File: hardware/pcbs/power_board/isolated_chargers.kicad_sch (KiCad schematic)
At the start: 9 parts, among them Q1 BSS138

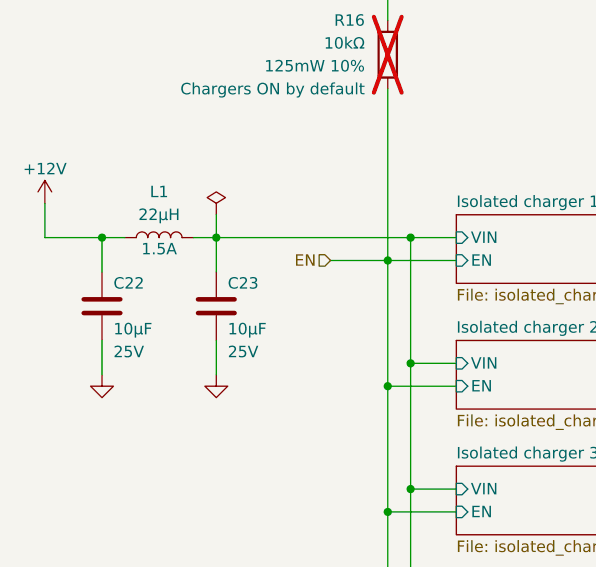
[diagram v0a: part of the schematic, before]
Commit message: power_board: arrange stuff on board
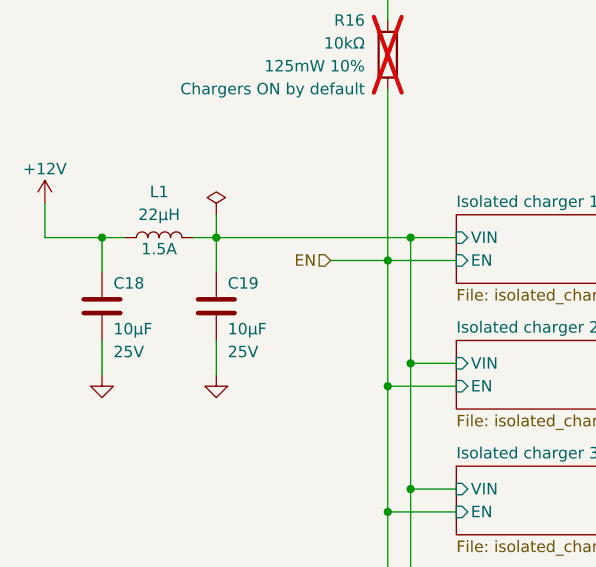
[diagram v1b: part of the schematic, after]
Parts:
- renumbered C22 to C18, C23 to C19
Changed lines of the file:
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@@
 		(dnp no)
 		(fields_autoplaced yes)
-		(property "Reference" "#PWR028"
+		(property "Reference" "#PWR024"
 			(at 160.02 78.74 0)
 			(effects
@@
 			(project "power_board"
 				(path "/4b166175-80a4-48c6-994d-6e62a6160b87/2e2b9578-5dbd-4b2d-88fb-256ac9c8dd75"
-					(reference "#PWR028")
+					(reference "#PWR024")
 					(unit 1)
 				)
@@
 		(on_board yes)
 		(dnp no)
-		(property "Reference" "C23"
+		(property "Reference" "C19"
 			(at 88.9 106.68 0)
 			(effects
@@
 			(project "power_board"
 				(path "/4b166175-80a4-48c6-994d-6e62a6160b87/2e2b9578-5dbd-4b2d-88fb-256ac9c8dd75"
-					(reference "C23")
+					(reference "C19")
 					(unit 1)
 				)
@@
 		(on_board yes)
 		(dnp no)
-		(property "Reference" "#PWR029"
+		(property "Reference" "#PWR025"
 			(at 185.42 78.74 0)
 			(effects
@@
 			(project "power_board"
 				(path "/4b166175-80a4-48c6-994d-6e62a6160b87/2e2b9578-5dbd-4b2d-88fb-256ac9c8dd75"
-					(reference "#PWR029")
+					(reference "#PWR025")
 					(unit 1)
 				)
@@
 		(dnp no)
 		(fields_autoplaced yes)
-		(property "Reference" "#PWR027"
+		(property "Reference" "#PWR023"
 			(at 106.68 172.72 0)
 			(effects
@@
 			(project "power_board"
 				(path "/4b166175-80a4-48c6-994d-6e62a6160b87/2e2b9578-5dbd-4b2d-88fb-256ac9c8dd75"
-					(reference "#PWR027")
+					(reference "#PWR023")
 					(unit 1)
 				)
@@
 		(dnp no)
 		(fields_autoplaced yes)
-		(property "Reference" "#PWR030"
+		(property "Reference" "#PWR026"
 			(at 185.42 114.3 0)
 			(effects
@@
 			(project "power_board"
 				(path "/4b166175-80a4-48c6-994d-6e62a6160b87/2e2b9578-5dbd-4b2d-88fb-256ac9c8dd75"
-					(reference "#PWR030")
+					(reference "#PWR026")
 					(unit 1)
 				)
@@
 		(on_board yes)
 		(dnp no)
-		(property "Reference" "#PWR026"
+		(property "Reference" "#PWR022"
 			(at 106.68 78.74 0)
 			(effects
@@
 			(project "power_board"
 				(path "/4b166175-80a4-48c6-994d-6e62a6160b87/2e2b9578-5dbd-4b2d-88fb-256ac9c8dd75"
-					(reference "#PWR026")
+					(reference "#PWR022")
 					(unit 1)
 				)
@@
 		(dnp no)
 		(fields_autoplaced yes)
-		(property "Reference" "#PWR024"
+		(property "Reference" "#PWR020"
 			(at 74.93 123.19 0)
 			(effects
@@
 			(project "power_board"
 				(path "/4b166175-80a4-48c6-994d-6e62a6160b87/2e2b9578-5dbd-4b2d-88fb-256ac9c8dd75"
-					(reference "#PWR024")
+					(reference "#PWR020")
 					(unit 1)
 				)
@@
 		(on_board yes)
 		(dnp no)
-		(property "Reference" "C22"
+		(property "Reference" "C18"
 			(at 76.2 106.68 0)
 			(effects
@@
 			(project "power_board"
 				(path "/4b166175-80a4-48c6-994d-6e62a6160b87/2e2b9578-5dbd-4b2d-88fb-256ac9c8dd75"
-					(reference "C22")
+					(reference "C18")
 					(unit 1)
 				)
@@
 		(dnp no)
 		(fields_autoplaced yes)
-		(property "Reference" "#PWR025"
+		(property "Reference" "#PWR021"
 			(at 87.63 123.19 0)
 			(effects
@@
 			(project "power_board"
 				(path "/4b166175-80a4-48c6-994d-6e62a6160b87/2e2b9578-5dbd-4b2d-88fb-256ac9c8dd75"
-					(reference "#PWR025")
+					(reference "#PWR021")
 					(unit 1)
 				)
@@
 		(on_board yes)
 		(dnp no)
-		(property "Reference" "#PWR023"
+		(property "Reference" "#PWR019"
 			(at 68.58 101.6 0)
 			(effects
@@
 			(project "power_board"
 				(path "/4b166175-80a4-48c6-994d-6e62a6160b87/2e2b9578-5dbd-4b2d-88fb-256ac9c8dd75"
-					(reference "#PWR023")
-					(unit 1)
-				)
+					(reference "#PWR019")
+					(unit 1)
+				)

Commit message: power_board: final version
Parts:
- C18, C19: LCSC (none) -> C15850
- L1: LCSC (none) -> C223014
- Q1: LCSC (none) -> C7420339
- R16, R17, R20: LCSC (none) -> C17414
- R18: LCSC (none) -> C17673
- R19: LCSC (none) -> C17415
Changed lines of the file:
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@@
+			)
+		)
+		(property "LCSC" "C7420339"
+			(at 182.88 101.6 0)
+			(effects
+				(font
+					(size 1.27 1.27)
+				)
+				(hide yes)
 			)
 		)
@@
 		)
 		(property "Shop" "https://store.comet.bg/Catalogue/Product/29580/"
+			(at 170.18 101.6 0)
+			(effects
+				(font
+					(size 1.27 1.27)
+				)
+				(hide yes)
+			)
+		)
+		(property "LCSC" "C17415"
 			(at 170.18 101.6 0)
 			(effects
@@
 			)
 		)
+		(property "LCSC" "C17414"
+			(at 106.68 160.02 0)
+			(effects
+				(font
+					(size 1.27 1.27)
+				)
+				(hide yes)
+			)
+		)
 		(pin "1"
 		)
@@
 		)
 		(property "Shop" "https://store.comet.bg/Catalogue/Product/44616/"
+			(at 87.63 109.22 0)
+			(effects
+				(font
+					(size 1.27 1.27)
+				)
+				(hide yes)
+			)
+		)
+		(property "LCSC" "C15850"
 			(at 87.63 109.22 0)
 			(effects
@@
 			)
 		)
+		(property "LCSC" "C17414"
+			(at 185.42 81.28 0)
+			(effects
+				(font
+					(size 1.27 1.27)
+				)
+				(hide yes)
+			)
+		)
 		(pin "1"
 		)
@@
 			)
 		)
+		(property "LCSC" "C15850"
+			(at 74.93 109.22 0)
+			(effects
+				(font
+					(size 1.27 1.27)
+				)
+				(hide yes)
+			)
+		)
 		(pin "1"
 		)
@@
 			)
 		)
+		(property "LCSC" "C17414"
+			(at 106.68 81.28 0)
+			(effects
+				(font
+					(size 1.27 1.27)
+				)
+				(hide yes)
+			)
+		)
 		(pin "1"
 		)
@@
 			)
 		)
+		(property "LCSC" "C17673"
+			(at 160.02 81.28 0)
+			(effects
+				(font
+					(size 1.27 1.27)
+				)
+				(hide yes)
+			)
+		)
 		(pin "1"
 		)
@@
 			)
 		)
+		(property "LCSC" "C223014"
+			(at 81.28 101.6 0)
+			(effects
+				(font
+					(size 1.27 1.27)
+				)
+				(hide yes)
+			)
+		)

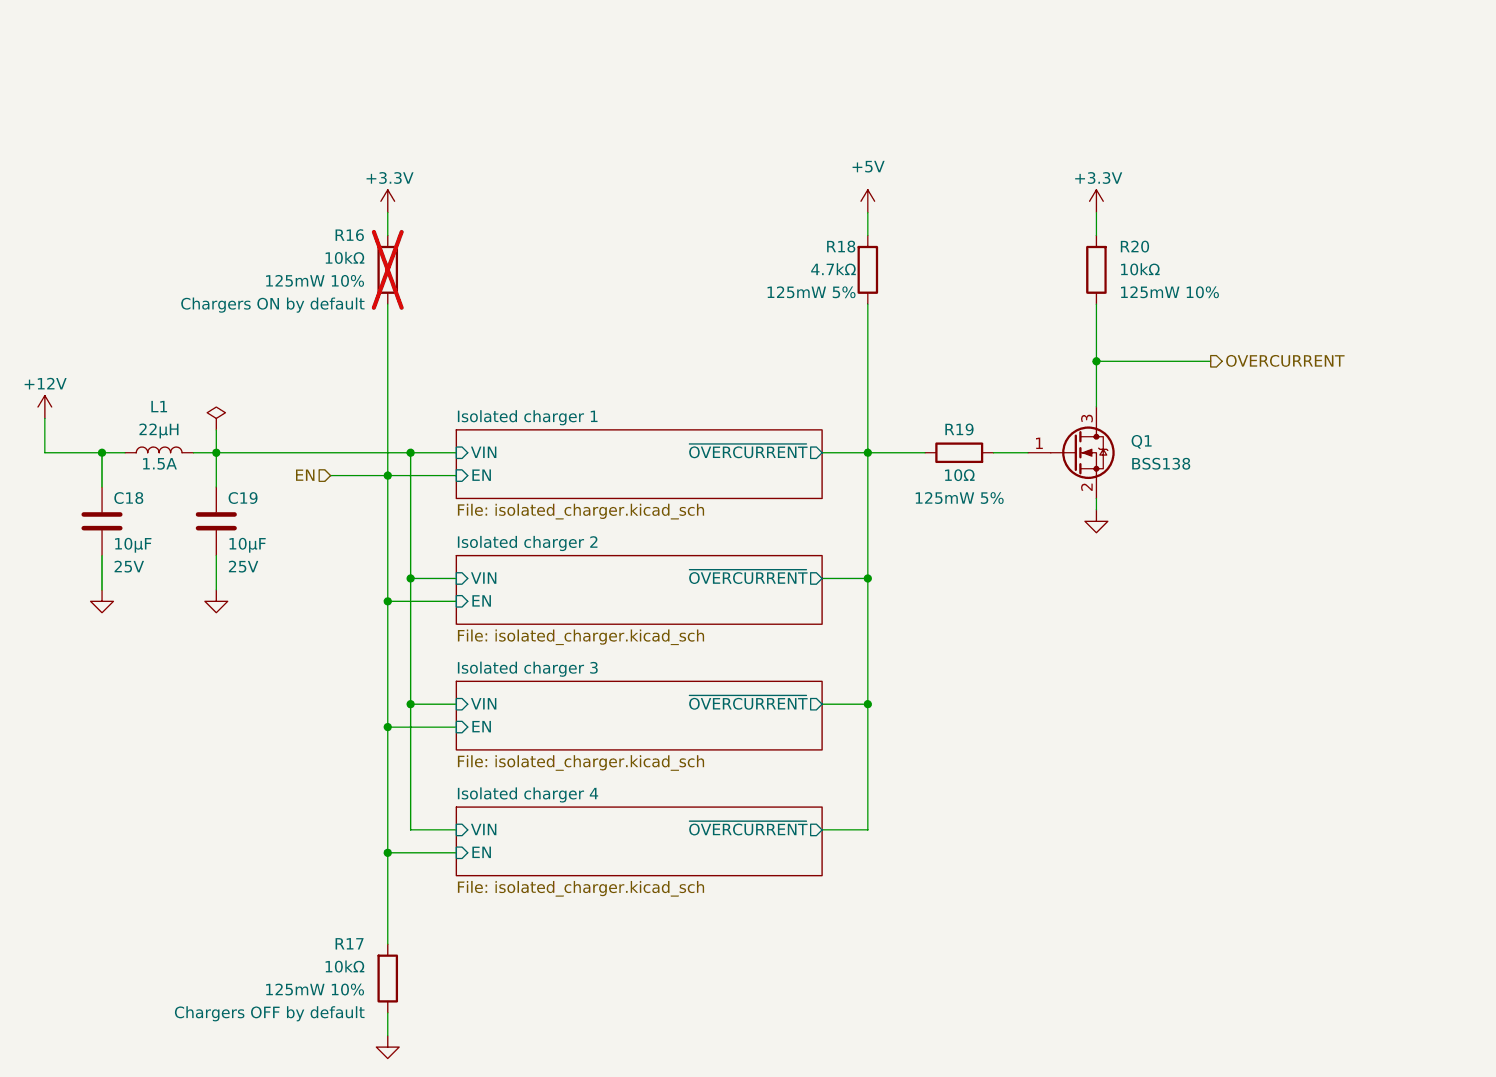
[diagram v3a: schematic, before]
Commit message: power_board: nuke general purpose leds and power cycler
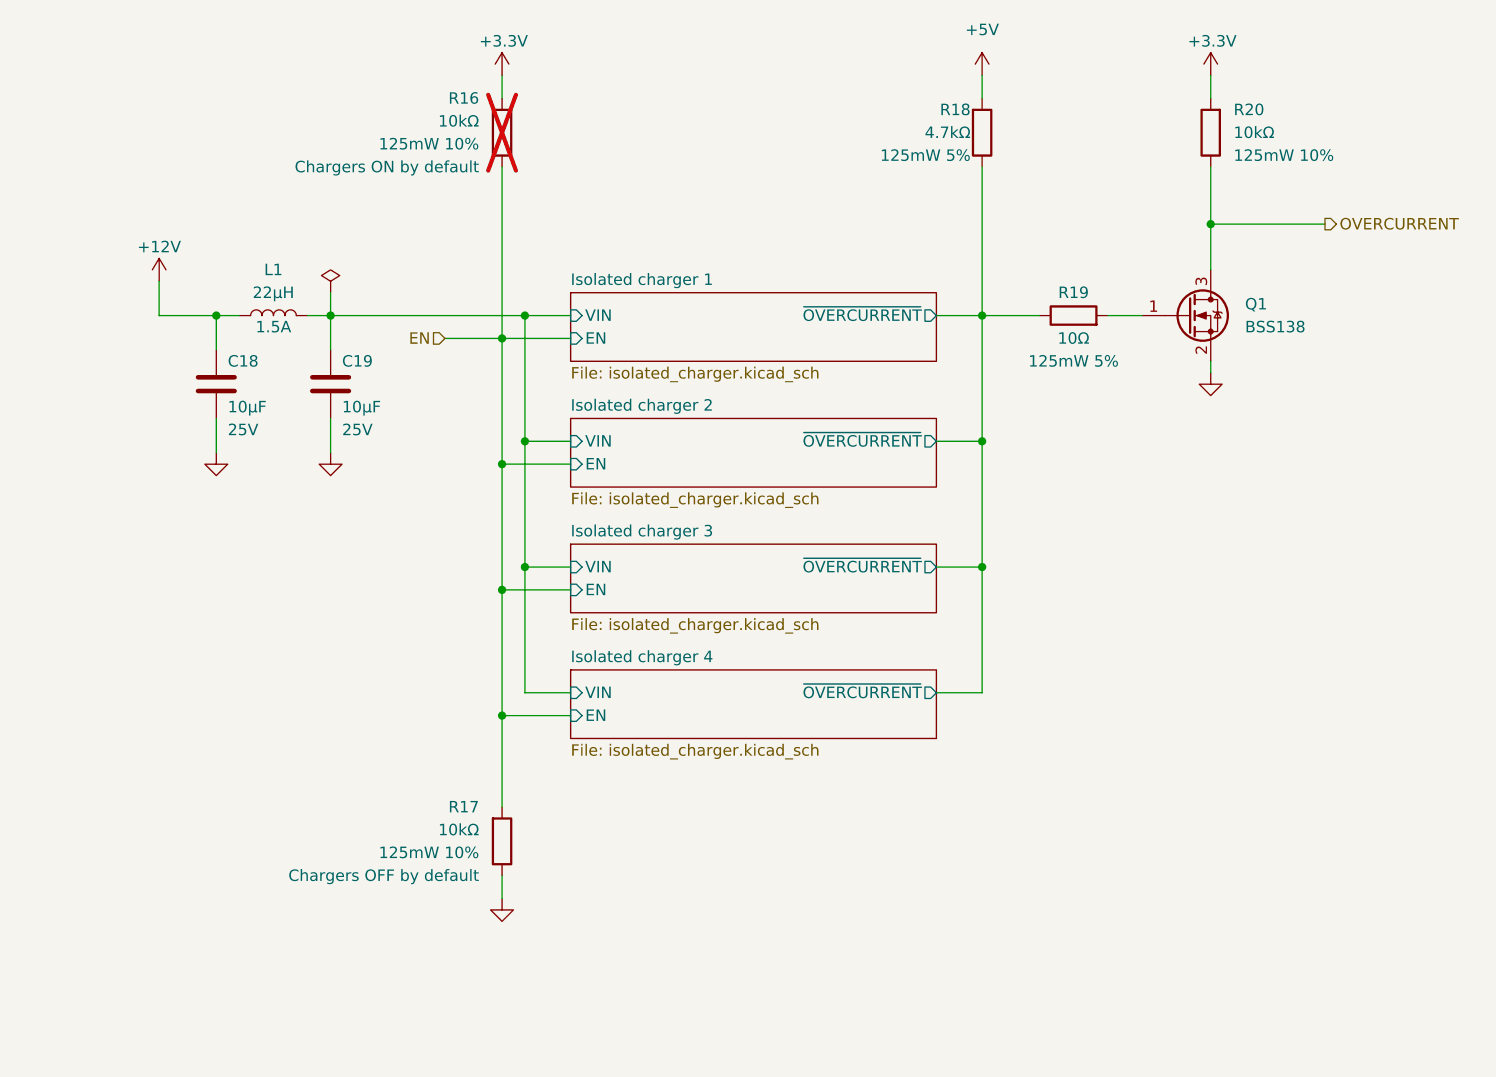
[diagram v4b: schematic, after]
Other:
- moved on the sheet: C18, C19, L1, Q1, R16, R17, R18, R19, R20

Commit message: power_board: update components to new versions and annotate
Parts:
- L1: Part (none) -> NRS6045T220MMGK
- Q1: Part (none) -> BSS138
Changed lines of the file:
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@@
+			)
+		)
+		(property "Part" "BSS138"
+			(at 195.58 86.36 0)
+			(effects
+				(font
+					(size 1.27 1.27)
+				)
+				(hide yes)
 			)
 		)
@@
 		(dnp no)
 		(fields_autoplaced yes)
-		(property "Reference" "#PWR024"
+		(property "Reference" "#PWR023"
 			(at 172.72 63.5 0)
 			(effects
@@
 			(project "power_board"
 				(path "/4b166175-80a4-48c6-994d-6e62a6160b87/2e2b9578-5dbd-4b2d-88fb-256ac9c8dd75"
-					(reference "#PWR024")
+					(reference "#PWR023")
 					(unit 1)
 				)
@@
 		(on_board yes)
 		(dnp no)
-		(property "Reference" "#PWR025"
+		(property "Reference" "#PWR024"
 			(at 198.12 63.5 0)
 			(effects
@@
 			(project "power_board"
 				(path "/4b166175-80a4-48c6-994d-6e62a6160b87/2e2b9578-5dbd-4b2d-88fb-256ac9c8dd75"
-					(reference "#PWR025")
+					(reference "#PWR024")
 					(unit 1)
 				)
@@
 		(dnp no)
 		(fields_autoplaced yes)
-		(property "Reference" "#PWR023"
+		(property "Reference" "#PWR022"
 			(at 119.38 157.48 0)
 			(effects
@@
 			(project "power_board"
 				(path "/4b166175-80a4-48c6-994d-6e62a6160b87/2e2b9578-5dbd-4b2d-88fb-256ac9c8dd75"
-					(reference "#PWR023")
+					(reference "#PWR022")
 					(unit 1)
 				)
@@
 		(dnp no)
 		(fields_autoplaced yes)
-		(property "Reference" "#PWR026"
+		(property "Reference" "#PWR025"
 			(at 198.12 99.06 0)
 			(effects
@@
 			(project "power_board"
 				(path "/4b166175-80a4-48c6-994d-6e62a6160b87/2e2b9578-5dbd-4b2d-88fb-256ac9c8dd75"
-					(reference "#PWR026")
+					(reference "#PWR025")
 					(unit 1)
 				)
@@
 		(on_board yes)
 		(dnp no)
-		(property "Reference" "#PWR022"
+		(property "Reference" "#PWR021"
 			(at 119.38 63.5 0)
 			(effects
@@
 			(project "power_board"
 				(path "/4b166175-80a4-48c6-994d-6e62a6160b87/2e2b9578-5dbd-4b2d-88fb-256ac9c8dd75"
-					(reference "#PWR022")
+					(reference "#PWR021")
 					(unit 1)
 				)
@@
 		(dnp no)
 		(fields_autoplaced yes)
-		(property "Reference" "#PWR020"
+		(property "Reference" "#PWR019"
 			(at 87.63 107.95 0)
 			(effects
@@
 			(project "power_board"
 				(path "/4b166175-80a4-48c6-994d-6e62a6160b87/2e2b9578-5dbd-4b2d-88fb-256ac9c8dd75"
-					(reference "#PWR020")
+					(reference "#PWR019")
 					(unit 1)
 				)
@@
 		(dnp no)
 		(fields_autoplaced yes)
-		(property "Reference" "#PWR021"
+		(property "Reference" "#PWR020"
 			(at 100.33 107.95 0)
 			(effects
@@
 			(project "power_board"
 				(path "/4b166175-80a4-48c6-994d-6e62a6160b87/2e2b9578-5dbd-4b2d-88fb-256ac9c8dd75"
-					(reference "#PWR021")
+					(reference "#PWR020")
 					(unit 1)
 				)
@@
 		(on_board yes)
 		(dnp no)
-		(property "Reference" "#PWR019"
+		(property "Reference" "#PWR018"
 			(at 81.28 86.36 0)
 			(effects
@@
 			(project "power_board"
 				(path "/4b166175-80a4-48c6-994d-6e62a6160b87/2e2b9578-5dbd-4b2d-88fb-256ac9c8dd75"
-					(reference "#PWR019")
+					(reference "#PWR018")
 					(unit 1)
 				)
@@
 			(at 93.98 86.36 0)
 			(effects
+				(font
+					(size 1.27 1.27)
+				)
+				(hide yes)
+			)
+		)
+		(property "Part" "NRS6045T220MMGK"
+			(at 93.98 86.36 0)
+			(effects
